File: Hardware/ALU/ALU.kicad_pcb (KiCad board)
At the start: 2 copper layers, 71.8 x 92.1 mm, 48 parts, among them J1 Conn_02x08_Odd_Even, J2 Conn_02x08_Odd_Even, J3 Conn_02x08_Odd_Even, U1 74x157, U10 74x32, U11 74x08, U12 74x377, U13 74x157, U14 74x157, U15 74x08, U16 74x32, U17 74x86, U18 74x157, U19 74x86, U2 74x86, U20 74x157, U21 74x283, U22 74x08, U23 74x32, U24 74x86, U25 74x157, U28 74x151, U29 74x151, U3 74x283, U30 74x151, U31 74x151, U4 74x151, U5 74x151, U6 74x151, U7 74x151, U8 74x86, U9 74x08

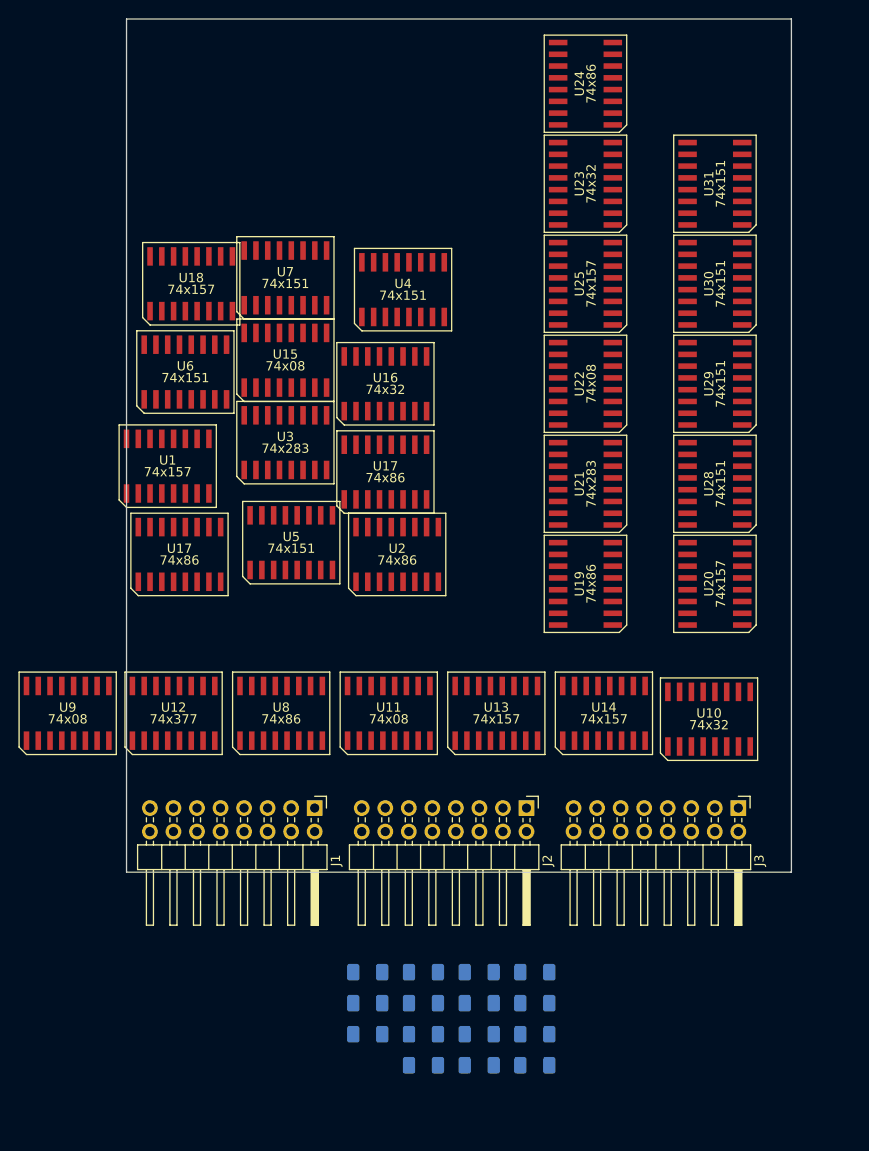
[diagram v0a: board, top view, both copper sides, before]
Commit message: ALU: About to increase modularity by moving opcode parsing out of ALU onto motherboard (would turn backplane into more of a motherboard).
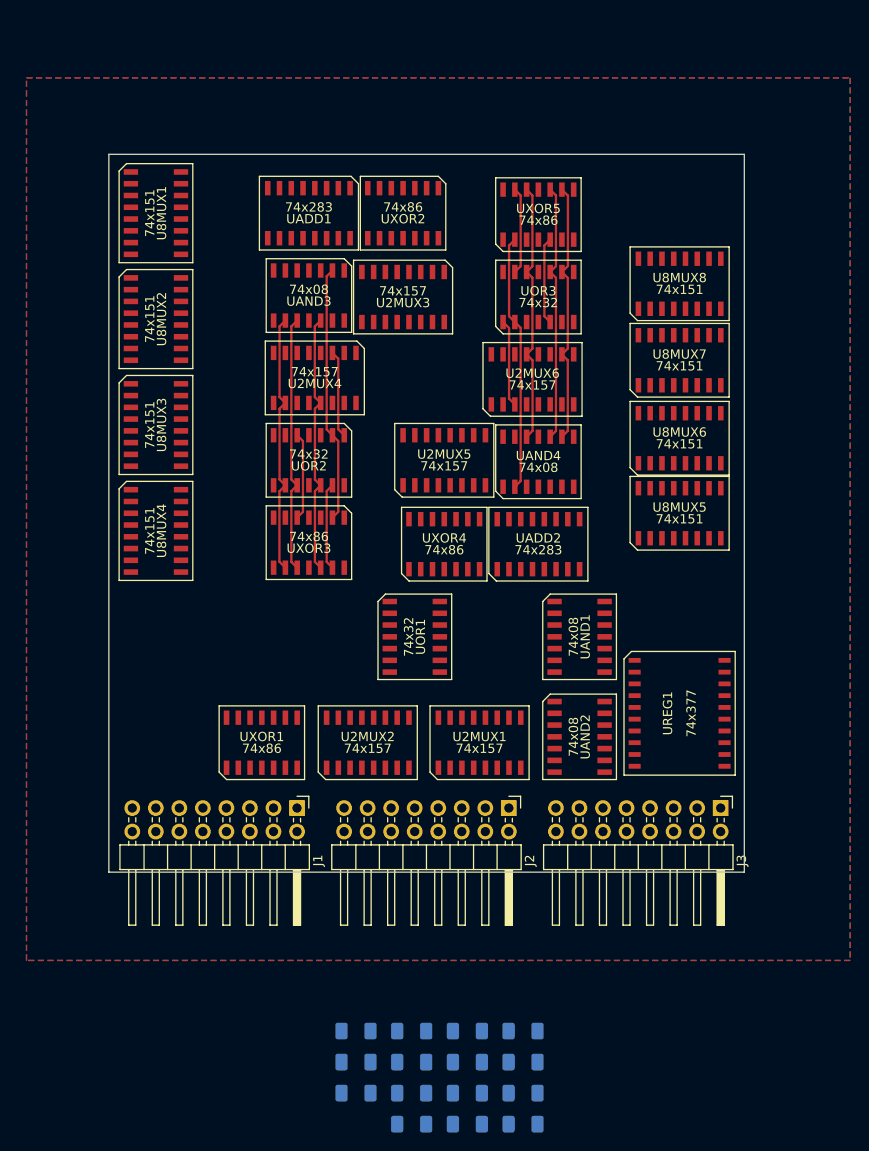
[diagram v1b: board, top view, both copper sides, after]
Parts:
- removed U1, U13, U14, U18, U20, U25: 74x157, 000custom:R-PDSO-G16
- removed U10, U16, U23: 74x32, 000custom:R-PDSO-G16
- removed U11, U15, U22, U9: 74x08, 000custom:R-PDSO-G16
- removed U12: 74x377, 000custom:R-PDSO-G16
- removed U17 (x2), U19, U2, U24, U8: 74x86, 000custom:R-PDSO-G16
- removed U21, U3: 74x283, 000custom:R-PDSO-G16
- removed U28, U29, U30, U31, U4, U5, U6, U7: 74x151, 000custom:R-PDSO-G16
- added U2MUX1: 74x157, 000custom:D_R-PDSO-G16, F.Cu at (125.1, 141.6)
- added U2MUX2: 74x157, 000custom:D_R-PDSO-G16, F.Cu at (113.0, 141.6)
- added U2MUX3: 74x157, 000custom:D_R-PDSO-G16, F.Cu at (116.8, 93.5)
- added U2MUX4: 74x157, 000custom:D_R-PDSO-G16, F.Cu at (107.3, 102.2)
- added U2MUX5: 74x157, 000custom:D_R-PDSO-G16, F.Cu at (121.3, 111.1)
- added U2MUX6: 74x157, 000custom:D_R-PDSO-G16, F.Cu at (130.8, 102.4)
- added U8MUX1: 74x151, 000custom:D_R-PDSO-G16, F.Cu at (90.2, 84.5)
- added U8MUX2: 74x151, 000custom:D_R-PDSO-G16, F.Cu at (90.2, 95.9)
- added U8MUX3: 74x151, 000custom:D_R-PDSO-G16, F.Cu at (90.2, 107.3)
- added U8MUX4: 74x151, 000custom:D_R-PDSO-G16, F.Cu at (90.2, 118.7)
- added U8MUX5: 74x151, 000custom:D_R-PDSO-G16, F.Cu at (146.7, 116.8)
- added U8MUX6: 74x151, 000custom:D_R-PDSO-G16, F.Cu at (146.7, 108.7)
- added U8MUX7: 74x151, 000custom:D_R-PDSO-G16, F.Cu at (146.7, 100.3)
- added U8MUX8: 74x151, 000custom:D_R-PDSO-G16, F.Cu at (146.7, 92.1)
- added UADD1: 74x283, 000custom:D_R-PDSO-G16, F.Cu at (106.7, 84.5)
- added UADD2: 74x283, 000custom:D_R-PDSO-G16, F.Cu at (131.4, 120.2)
- added UAND1: 74x08, 000custom:D_R-PDSO-G14, F.Cu at (135.9, 130.2)
- added UAND2: 74x08, 000custom:D_R-PDSO-G14, F.Cu at (135.9, 141.0)
- added UAND3: 74x08, 000custom:D_R-PDSO-G14, F.Cu at (106.7, 93.3)
- added UAND4: 74x08, 000custom:D_R-PDSO-G14, F.Cu at (131.4, 111.3)
- added UOR1: 74x32, 000custom:D_R-PDSO-G14, F.Cu at (118.1, 130.2)
- added UOR2: 74x32, 000custom:D_R-PDSO-G14, F.Cu at (106.7, 111.1)
- added UOR3: 74x32, 000custom:D_R-PDSO-G14, F.Cu at (131.4, 93.5)
- added UREG1: 74x377, 000custom:ON-SOIC20-WB, F.Cu at (146.7, 138.4)
- added UXOR1: 74x86, 000custom:D_R-PDSO-G14, F.Cu at (101.6, 141.6)
- added UXOR2: 74x86, 000custom:D_R-PDSO-G14, F.Cu at (116.8, 84.5)
- added UXOR3: 74x86, 000custom:D_R-PDSO-G14, F.Cu at (106.7, 120.0)
- added UXOR4: 74x86, 000custom:D_R-PDSO-G14, F.Cu at (121.3, 120.2)
- added UXOR5: 74x86, 000custom:D_R-PDSO-G14, F.Cu at (131.4, 84.6)
- J1, J2, J3: value Conn_02x08_Odd_Even -> connector_2x8
- moved C11 6.48 mm to (117.8, 182.8)
- moved C13 6.48 mm to (129.8, 182.8)
- moved C4 6.48 mm to (123.8, 182.8)
- moved C1 6.48 mm to (117.8, 179.4)
- moved C14 6.48 mm to (129.8, 172.7)
- moved C15 6.48 mm to (129.8, 176.1)
- moved C3 6.48 mm to (129.8, 179.4)
- moved C6 6.48 mm to (117.8, 172.7)
- moved C9 6.48 mm to (117.8, 176.1)
- moved C10 6.48 mm to (111.8, 176.1)
- moved C12 6.48 mm to (111.8, 179.4)
- moved C2 6.48 mm to (123.8, 172.7)
- moved C5 6.48 mm to (123.8, 179.4)
- moved C7 6.48 mm to (111.8, 172.7)
- moved C8 6.48 mm to (123.8, 176.1)
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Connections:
- J1 pad 11: /ACCHIGH1 -> /IN_ACC5
- J1 pad 13: /ACCHIGH2 -> /IN_ACC6
- J1 pad 15: /ACCHIGH3 -> /IN_ACC7
- J1 pad 9: /ACCHIGH0 -> /IN_ACC4
- J2 pad 5: /IMMHIGH0 -> /IN_OPCODE2
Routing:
- net /IN_ACC2: track 0.00 -> 28.3 mm
- net /IN_ACC6: track 0.00 -> 28.3 mm
- net /IN_ACC3: track 0.00 -> 28.2 mm
- net /IN_ACC7: track 0.00 -> 28.2 mm
- net /upper/OPERANDB0: track 0.00 -> 27.7 mm
- net /lower/OPERANDB2: track 0.00 -> 27.7 mm
- net /lower/OPERANDB0: track 0.00 -> 27.7 mm
- net /upper/OPERANDB2: track 0.00 -> 27.7 mm
- net /IN_ACC4: track 0.00 -> 9.42 mm
- net /IN_ACC0: track 0.00 -> 9.42 mm
- net /upper/OPERANDB3: track 0.00 -> 9.41 mm
- net /upper/OPERANDB1: track 0.00 -> 9.41 mm
- net /lower/OPERANDB3: track 0.00 -> 9.41 mm
- net /lower/OPERANDB1: track 0.00 -> 9.41 mm
- added copper zone on F.Cu, net GND
- added copper zone on In1.Cu, net GND
- added copper zone on In2.Cu, net GND
- added copper zone on B.Cu, net VCC
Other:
- board size 71.8 x 92.1 mm -> 68.6 x 77.5 mm
- copper layers 2 -> 4

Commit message: ALU: Starting routing. Also passing this to kicad's github #collab
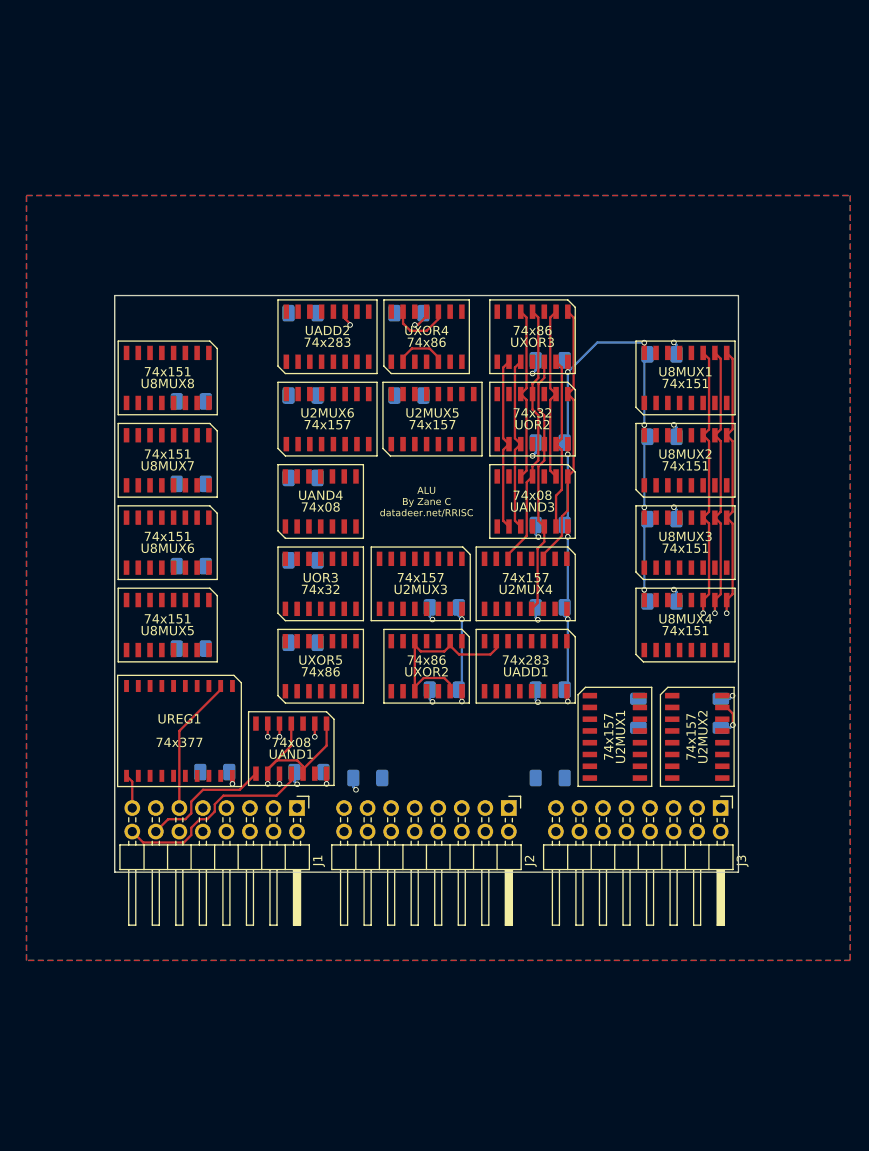
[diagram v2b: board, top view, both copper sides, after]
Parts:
- removed UAND2: 74x08, 000custom:D_R-PDSO-G14
- removed UOR1: 74x32, 000custom:D_R-PDSO-G14
- removed UXOR1: 74x86, 000custom:D_R-PDSO-G14
- added C16: .1uF, Capacitor_SMD:C_1206_3216Metric_Pad1.33x1.80mm_HandSolder, B.Cu at (144.8, 99.7)
- added C17: .1uF, Capacitor_SMD:C_1206_3216Metric_Pad1.33x1.80mm_HandSolder, B.Cu at (144.8, 117.5)
- added C18: .1uF, Capacitor_SMD:C_1206_3216Metric_Pad1.33x1.80mm_HandSolder, B.Cu at (106.0, 113.0)
- added C19: .1uF, Capacitor_SMD:C_1206_3216Metric_Pad1.33x1.80mm_HandSolder, B.Cu at (106.0, 95.2)
- added C20: .1uF, Capacitor_SMD:C_1206_3216Metric_Pad1.33x1.80mm_HandSolder, B.Cu at (106.0, 130.8)
- added C21: .1uF, Capacitor_SMD:C_1206_3216Metric_Pad1.33x1.80mm_HandSolder, B.Cu at (94.0, 122.6)
- added C22: .1uF, Capacitor_SMD:C_1206_3216Metric_Pad1.33x1.80mm_HandSolder, B.Cu at (106.0, 121.9)
- added C23: .1uF, Capacitor_SMD:C_1206_3216Metric_Pad1.33x1.80mm_HandSolder, B.Cu at (117.5, 95.2)
- added C24: .1uF, Capacitor_SMD:C_1206_3216Metric_Pad1.33x1.80mm_HandSolder, B.Cu at (117.5, 104.1)
- added C25: .1uF, Capacitor_SMD:C_1206_3216Metric_Pad1.33x1.80mm_HandSolder, B.Cu at (94.0, 104.8)
- added C26: .1uF, Capacitor_SMD:C_1206_3216Metric_Pad1.33x1.80mm_HandSolder, B.Cu at (106.0, 104.1)
- added C27: .1uF, Capacitor_SMD:C_1206_3216Metric_Pad1.33x1.80mm_HandSolder, B.Cu at (94.0, 131.4)
- added C28: .1uF, Capacitor_SMD:C_1206_3216Metric_Pad1.33x1.80mm_HandSolder, B.Cu at (94.0, 113.7)
- moved C9 77.2 mm to (132.7, 100.3)
- moved C10 75.1 mm to (144.8, 108.6), turned to 0 degrees
- moved C11 75.1 mm to (132.7, 109.2)
- moved U8MUX1 59.9 mm to (147.3, 102.2), turned to 0 degrees
- moved U8MUX2 59.1 mm to (147.3, 111.1), turned to 0 degrees
- moved U8MUX3 58.5 mm to (147.3, 120.0), turned to 0 degrees
- moved C7 58.5 mm to (132.7, 118.1)
- moved U8MUX4 58.0 mm to (147.3, 128.9), turned to 0 degrees
- moved U8MUX5 56.5 mm to (91.4, 128.9), turned to 180 degrees
- moved C13 56.4 mm to (121.3, 127.0)
- moved U8MUX6 56.4 mm to (91.4, 120.0), turned to 180 degrees
- moved U8MUX7 56.3 mm to (91.4, 111.1), turned to 180 degrees
- moved U8MUX8 56.2 mm to (91.4, 102.2), turned to 180 degrees
- moved UADD1 54.2 mm to (130.1, 133.3)
- moved UXOR5 54.1 mm to (108.0, 133.3)
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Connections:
- J1 pad 1: /IN_ACC0 -> VCC
- J1 pad 10: /IN_REGDATA4 -> /OUT_RX_ID0
- J1 pad 11: /IN_ACC5 -> /OUT_CARRY
- J1 pad 12: /IN_REGDATA5 -> /OUT_RX_ID1
- J1 pad 13: /IN_ACC6 -> GND
- J1 pad 14: /IN_REGDATA6 -> /OUT_RX_ID2
- J1 pad 15: /IN_ACC7 -> /CLK
- J1 pad 16: /IN_REGDATA7 -> /OUT_RX_ID3
- J1 pad 2: /IN_REGDATA0 -> /IN_IMMEDIATE0
- J1 pad 3: /IN_ACC1 -> GND
- J1 pad 4: /IN_REGDATA1 -> /IN_IMMEDIATE1
- J1 pad 5: /IN_ACC2 -> /CHANGEOUT
- J1 pad 6: /IN_REGDATA2 -> /IN_IMMEDIATE2
- J1 pad 7: /IN_ACC3 -> /~{CARRY_WE}
- J1 pad 8: /IN_REGDATA3 -> /IN_IMMEDIATE3
- J1 pad 9: /IN_ACC4 -> /SWAP_NIBBLES
- J2 pad 1: /IN_OPCODE0 -> /IN_ACC0
- J2 pad 10: /OUT_RESULT4 -> /IN_REGDATA4
- J2 pad 11: /IN_IMMEDIATE1 -> /IN_ACC5
- J2 pad 12: /OUT_RESULT5 -> /IN_REGDATA5
- J2 pad 13: /IN_IMMEDIATE2 -> /IN_ACC6
- J2 pad 14: /OUT_RESULT6 -> /IN_REGDATA6
- J2 pad 15: /IN_IMMEDIATE3 -> /IN_ACC7
- J2 pad 16: /OUT_RESULT7 -> /IN_REGDATA7
- J2 pad 2: /OUT_RESULT0 -> /IN_REGDATA0
- J2 pad 3: /IN_OPCODE1 -> /IN_ACC1
- J2 pad 4: /OUT_RESULT1 -> /IN_REGDATA1
- J2 pad 5: /IN_OPCODE2 -> /IN_ACC2
- J2 pad 6: /OUT_RESULT2 -> /IN_REGDATA2
- J2 pad 7: /IN_OPCODE3 -> /IN_ACC3
- J2 pad 8: /OUT_RESULT3 -> /IN_REGDATA3
- J2 pad 9: /IN_IMMEDIATE0 -> /IN_ACC4
- J3 pad 1: /CLK -> /IN_OPCODE3
- J3 pad 10: /OUT_RX_ID0 -> /OUT_RESULT3
- J3 pad 12: /OUT_RX_ID1 -> /OUT_RESULT2
- J3 pad 14: /OUT_RX_ID2 -> /OUT_RESULT1
- J3 pad 16: /OUT_RX_ID3 -> /OUT_RESULT0
- J3 pad 2: GND -> /OUT_RESULT7
- J3 pad 3: /OUT_CARRY -> /IN_OPCODE2
- J3 pad 4: GND -> /OUT_RESULT6
- J3 pad 5: GND -> /IN_OPCODE1
- J3 pad 6: GND -> /OUT_RESULT5
- J3 pad 7: GND -> /IN_OPCODE0
- J3 pad 8: GND -> /OUT_RESULT4
- U8MUX1 pad 13: /IN_ACC0 -> GND
- U8MUX2 pad 13: /IN_ACC1 -> GND
- U8MUX3 pad 13: /IN_ACC2 -> GND
- U8MUX4 pad 13: /IN_ACC3 -> GND
- U8MUX5 pad 13: /IN_ACC4 -> GND
- U8MUX6 pad 13: /IN_ACC5 -> GND
- U8MUX7 pad 13: /IN_ACC6 -> GND
- U8MUX8 pad 13: /IN_ACC7 -> GND
- UAND1 pad 1: /IN_OPCODE1 -> /CHANGEOUT
- UAND1 pad 2: /IN_OPCODE2 -> /IN_IMMEDIATE0
- UAND1 pad 3: /OP2AND1 -> /OUT_RX_ID0
- UAND1 pad 4: /OP2AND1 -> /CHANGEOUT
- UAND1 pad 5: Net-(UOR1-Pad11) -> /IN_IMMEDIATE1
- UAND1 pad 6: /CHANGEOUT -> /OUT_RX_ID1
- UREG1 pad 1: Net-(UOR1-Pad3) -> /~{CARRY_WE}
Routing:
- net VCC: track 0.00 -> 115.8 mm, vias 0 -> 14
- net /IN_OPCODE1: track 0.00 -> 87.7 mm, vias 0 -> 1
- net /IN_OPCODE2: track 0.00 -> 51.5 mm, vias 0 -> 1
- net /IN_OPCODE3: track 0.00 -> 51.0 mm, vias 0 -> 1
- net /IN_ACC1: track 0.00 -> 28.8 mm
- net /IN_ACC6: track 28.3 -> 0.00 mm
- net /IN_ACC7: track 28.2 -> 0.00 mm
- net /upper/OPERANDB0: track 27.7 -> 0.00 mm
- net /upper/OPERANDB2: track 27.7 -> 0.00 mm
- net /CHANGEOUT: track 0.00 -> 24.1 mm, vias 0 -> 1
- net GND: track 0.00 -> 22.8 mm, vias 0 -> 14
- net /OUT_RX_ID3: track 0.00 -> 22.1 mm
- net /IN_ACC0: track 9.42 -> 28.8 mm
- net /OUT_RX_ID1: track 0.00 -> 18.2 mm, vias 0 -> 1
- net /OUT_CARRY: track 0.00 -> 15.0 mm
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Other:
- board size 68.6 x 77.5 mm -> 67.3 x 62.2 mm
- board text added: "ALU By Zane C datadeer.net/RRISC"

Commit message: ALU: Routing Progress
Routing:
- net /PRESWAPPED1: track 0.00 -> 59.5 mm, vias 0 -> 2
- net /SWAP_NIBBLES: track 0.00 -> 57.5 mm, vias 0 -> 1
- net /PRESWAPPED2: track 0.00 -> 55.7 mm, vias 0 -> 2
- net /PRESWAPPED0: track 0.00 -> 54.1 mm, vias 0 -> 2
- net /PRESWAPPED3: track 0.00 -> 52.4 mm, vias 0 -> 2
- net /IN_OPCODE0: track 0.00 -> 49.4 mm, vias 0 -> 3
- net /IN_OPCODE1: track 87.7 -> 132.7 mm, vias 1 -> 3
- net /IN_ACC2: track 18.8 -> 62.5 mm, vias 0 -> 2
- net /IN_REGDATA2: track 0.00 -> 42.2 mm, vias 0 -> 2
- net /IN_REGDATA3: track 0.00 -> 41.3 mm, vias 0 -> 2
- net /IN_ACC1: track 28.8 -> 63.2 mm, vias 0 -> 2
- net /lower/OPERANDB2: track 18.8 -> 53.1 mm, vias 0 -> 2
- net /IN_IMMEDIATE0: track 12.5 -> 46.1 mm, vias 1 -> 3
- net /IN_IMMEDIATE1: track 12.5 -> 44.8 mm, vias 1 -> 3
- net /IN_ACC3: track 28.3 -> 58.2 mm, vias 0 -> 1
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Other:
- board text added: "ALU By Zane C"
- board text removed: "ALU By Zane C datadeer.net/RRISC"

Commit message: Logisim: Saving before replacing ALU with mux-based-alu and before replacing von-neumann-based memory with harvard-based memory
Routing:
- net /IN_OPCODE2: track 51.8 -> 196.1 mm, vias 1 -> 7
- net GND: track 43.6 -> 178.8 mm, vias 23 -> 50
- net VCC: track 115.6 -> 219.9 mm, vias 14 -> 26
- net /IN_OPCODE3: track 51.0 -> 145.3 mm, vias 1 -> 3
- net /IN_OPCODE1: track 132.7 -> 216.1 mm, vias 3 -> 7
- net /IN_ACC4: track 0.00 -> 63.3 mm, vias 0 -> 4
- net /IN_ACC5: track 0.00 -> 62.1 mm, vias 0 -> 2
- net /upper/OPERANDB3: track 0.00 -> 58.2 mm, vias 0 -> 3
- net /IN_ACC7: track 0.00 -> 57.6 mm
- net /upper/OPERANDB2: track 0.00 -> 53.1 mm, vias 0 -> 2
- net /upper/OPERANDB1: track 0.00 -> 49.1 mm, vias 0 -> 2
- net /IN_ACC6: track 0.00 -> 41.6 mm, vias 0 -> 2
- net /lower/OP5_BIT3: track 0.00 -> 38.3 mm, vias 0 -> 3
- net /upper/OP5_BIT3: track 0.00 -> 38.3 mm, vias 0 -> 3
- net /upper/OP0_BIT0: track 0.00 -> 37.1 mm, vias 0 -> 2
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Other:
- board text added: "ALU By Zane C datadeer.net/RRISC"
- board text removed: "ALU By Zane C"
